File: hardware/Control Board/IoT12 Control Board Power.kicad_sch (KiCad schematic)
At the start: 21 parts, among them U5 LM2596S-ADJ, U7 MAX809S

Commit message: Start of next iteration.
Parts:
- removed C33, C34: 100nF, Capacitor_SMD:C_0805_2012Metric_Pad1.18x1.45mm_HandSolder, symbol Device:C
- removed C70, C71: 100uF/35V, Capacitor_SMD:CP_Elec_6.3x7.7, symbol Device:C_Polarized
- removed D6, D7: SS34, Diode_SMD:D_SMA, symbol Device:D_Schottky
- removed F1: *see schematic., Fuse:Fuse_Bourns_MF-RG1000, symbol Device:Polyfuse
- removed F2: 0.5A/30V, Fuse:Fuse_Bourns_MF-RG400, symbol Device:Polyfuse
- removed J6, J7, J8: ~, TestPoint:TestPoint_THTPad_D2.0mm_Drill1.0mm, symbol Connector_Generic:Conn_01x01
- removed L1: 68uH, Inductor-fixed:L_12x12mm_H8mm, symbol Device:L
- removed R52: 4k7 1%, Resistor_SMD:R_0805_2012Metric_Pad1.20x1.40mm_HandSolder, symbol Device:R
- removed U5: LM2596S-ADJ, Package_TO_SOT_SMD:TO-263-5_TabPin3, symbol Regulator_Switching:LM2596S-ADJ
- added D3: BAV99, Package_TO_SOT_SMD:SOT-23, symbol Diode:BAV99
- added J4: JST B4B-XH-A, Connector_JST:JST_XH_B4B-XH-A_1x04_P2.50mm_Vertical, symbol Connector:Conn_01x04_Male
- added R2: 100R, Resistor_SMD:R_0805_2012Metric_Pad1.20x1.40mm_HandSolder, symbol Device:R
- R40: value 3k3 -> 4k7 1%
- R73: value 100K -> 100k
- renumbered D12 to D4, U7 to U5
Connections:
- net +24V: now also J4.1 (Pin_1)
- net +5V: now also J4.2 (Pin_2); no longer R40.1
- net GND: now also R40.1, J4.3 (Pin_3); no longer R31.1
- net VIN: now also R40.2
- net at R31.2: now also J4.4 (Pin_4); no longer R40.2
- net at D4.3 (K), R73.1, U5.2 (~{RESET}): now also D3.3 (K)
- new net: D3.1 (K), R2.1
- new net 24V_ON: R31.1
- new net SAMD21_~{RESET}: R2.2
- no-connect marks 1 -> 2
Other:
- note added: "Power input"
- note removed: "*F1: fuse must be <=50% of amperage of T12 tip. Fuse Vmax must exceed Vsupply. Power supply must be >=100% of amperage of T12 tip. MPM-90-24: 1.50A (JK60-150) MPM-30-15: 0.90A MPM-20-12: 0.75A"
- note removed: "Max 24V DC"
- note removed: "Power supply"
- company: (none) -> https://github.com/atoomnetmarc/IoT12
- title: IoT12-hardware power supply -> IoT12 Control Board
- moved on the sheet: D4, R12, R73, U5

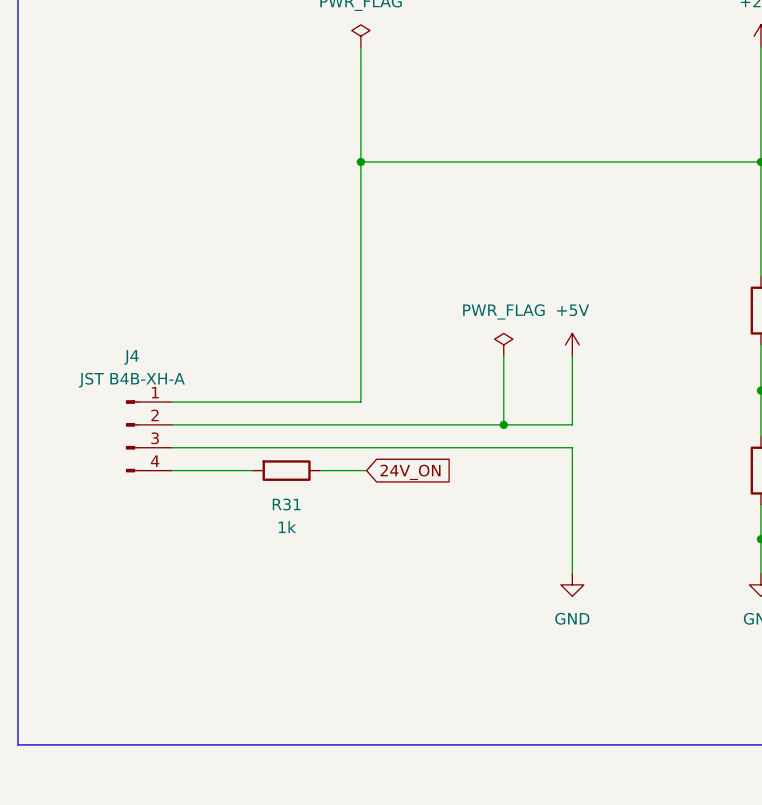
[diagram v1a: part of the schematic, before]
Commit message: Update Control Board project to Kicad 7.0.2
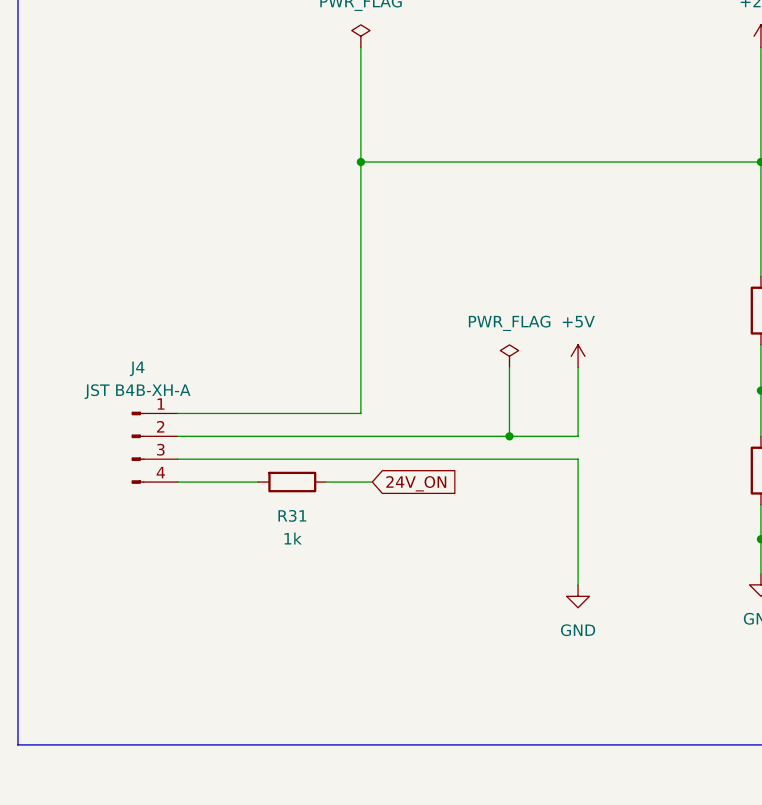
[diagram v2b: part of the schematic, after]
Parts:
- J4: symbol Connector:Conn_01x04_Male -> Connector:Conn_01x04_Pin
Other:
- moved on the sheet: J4, R31
